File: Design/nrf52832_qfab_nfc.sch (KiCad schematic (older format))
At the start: 23 parts, among them U1 nRF52832_QFAB, X1 32MHz, X2 32.768kHz

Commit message: Improvement over the Power management: - added TPS6201DRC for raising leaking voltage from supercapacitor - supercap is protected from overvoltage using a shunt diode - power management is using MOSFET logic (2 PFET, 1 NFET)
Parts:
- renumbered C13 to C11, C14 to C12, C8 to C13, C3 to C14, C2 to C15, C1 to C16, C7 to C17, C6 to C18, C11 to C5, C12 to C6, C4 to C7, C9 to C8, C5 to C9, L2 to L4, L1 to L5, U1 to U3, X2 to X1, X1 to X2
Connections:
- net labels added: CPU_SWD_CLK, CPU_SWD_IO, CPU_SWD_~RESET~, CPU_UART_CTS, CPU_UART_RTS, CPU_UART_RX, CPU_UART_TX, Energy_NFC_1, Energy_NFC_2, LED_PWM_B, LED_PWM_G, LED_PWM_R, Memory_SPI_CLK, Memory_SPI_MISO, Memory_SPI_MOSI, Memory_SPI_~CS~, Memory_SPI_~HOLD~, Memory_SPI_~WP~
- wire segments 96 -> 100
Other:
- moved on the sheet: C_tune1

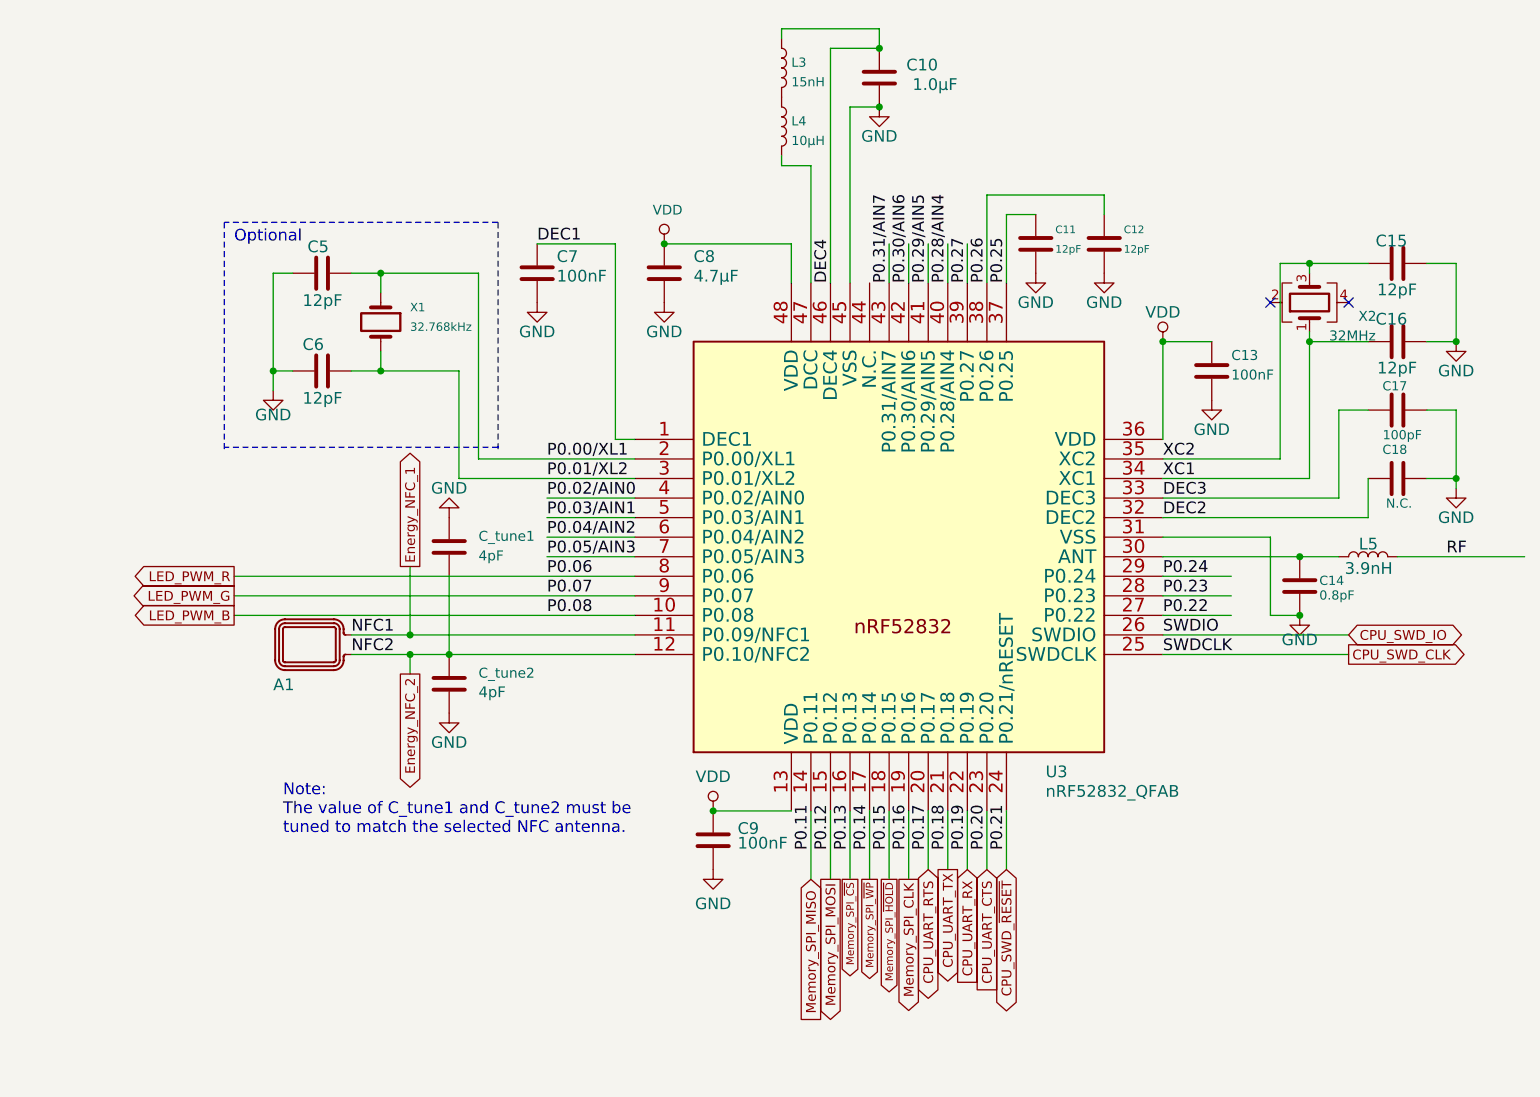
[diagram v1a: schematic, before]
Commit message: - designed configurable intensity for RGB LEDs - included Breakout (FET, Diode, etc.) Spice models from Cadence Spice - replaced global label with hierarchical complete view - customized net labels with pin function - exported first spice netlist which presents small bugs
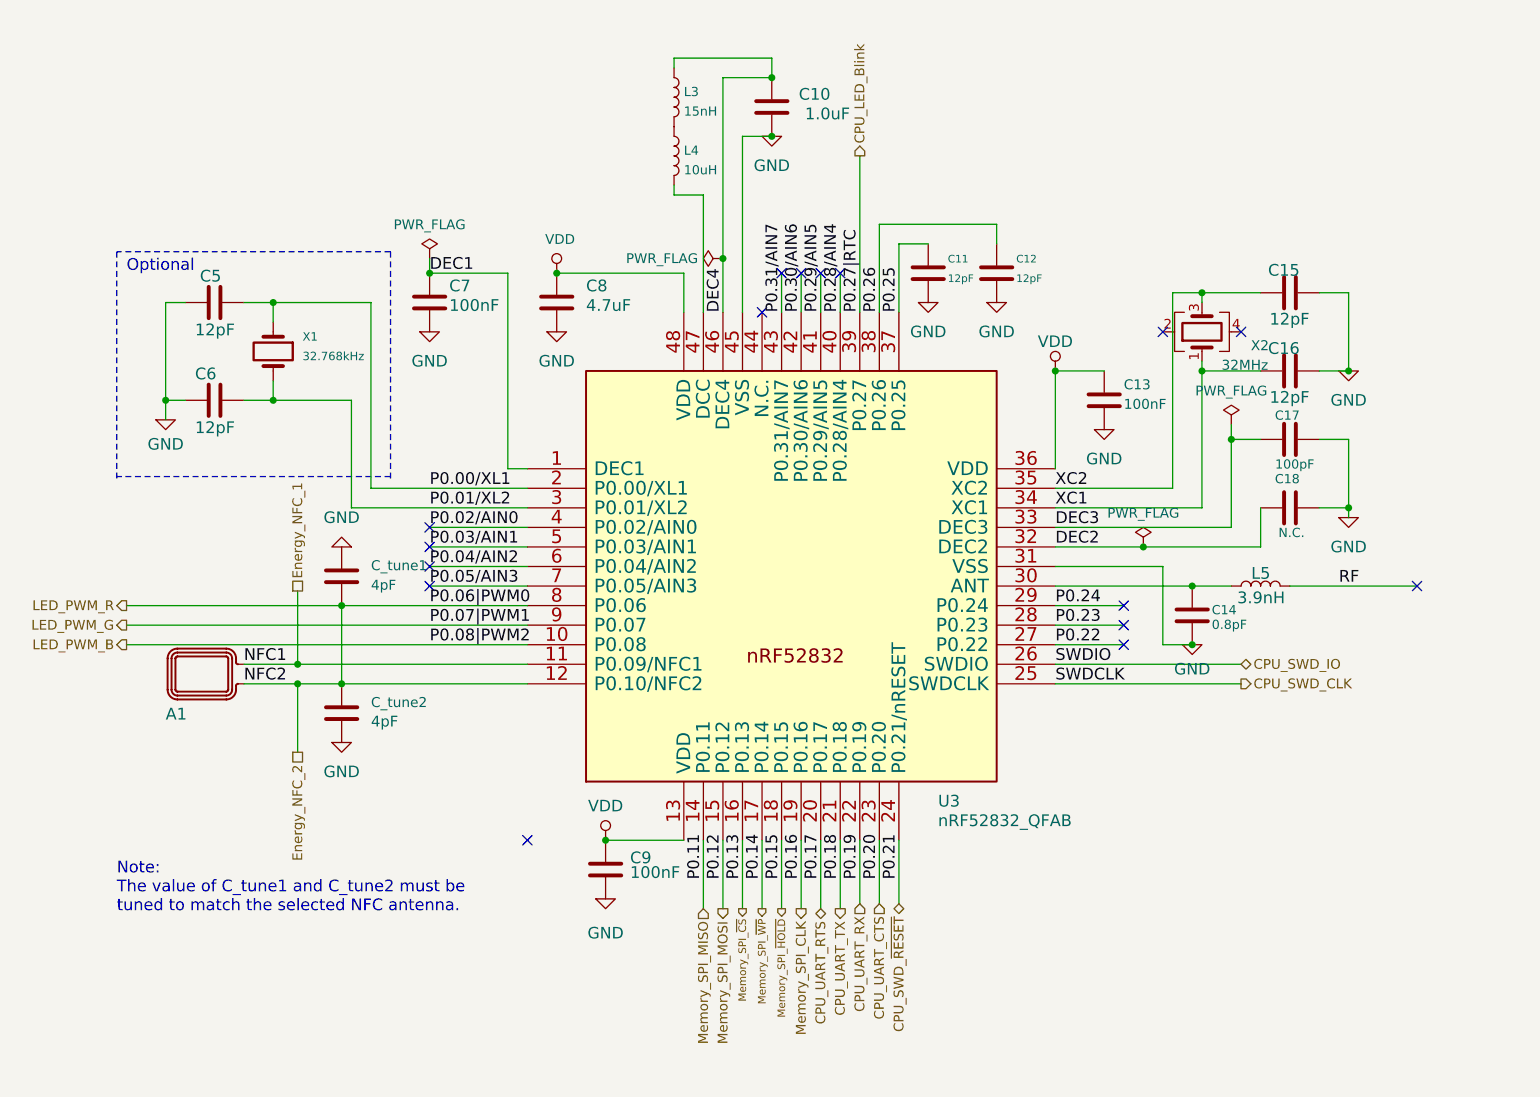
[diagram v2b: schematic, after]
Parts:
- A1: Spice_Model (none) -> 0; Spice_Netlist_Enabled (none) -> N; Spice_Primitive (none) -> L
- C10: value 1.0µF -> 1.0uF; Spice_Model (none) -> 1.0u; Spice_Netlist_Enabled (none) -> Y; Spice_Primitive (none) -> C
- C11, C12, C15, C16, C5, C6: Spice_Model (none) -> 12p; Spice_Netlist_Enabled (none) -> Y; Spice_Primitive (none) -> C
- C13, C7, C9: Spice_Model (none) -> 100n; Spice_Netlist_Enabled (none) -> Y; Spice_Primitive (none) -> C
- C14: Spice_Model (none) -> 0.8; Spice_Netlist_Enabled (none) -> Y; Spice_Primitive (none) -> C
- C17: Spice_Model (none) -> 100p; Spice_Netlist_Enabled (none) -> Y; Spice_Primitive (none) -> C
- C18: Spice_Model (none) -> 0; Spice_Netlist_Enabled (none) -> N; Spice_Primitive (none) -> C
- C8: value 4.7µF -> 4.7uF; Spice_Model (none) -> 4.7u; Spice_Netlist_Enabled (none) -> Y; Spice_Primitive (none) -> C
- C_tune1, C_tune2: Spice_Model (none) -> 4p; Spice_Netlist_Enabled (none) -> Y; Spice_Primitive (none) -> C
- L4: value 10µH -> 10uH; Spice_Model (none) -> 10u; Spice_Netlist_Enabled (none) -> Y; Spice_Primitive (none) -> L
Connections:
- net labels added: CPU_LED_Blink, P0.06|PWM0, P0.07|PWM1, P0.08|PWM2, P0.27|RTC
- net labels removed: P0.06, P0.07, P0.08, P0.27
- wire segments 100 -> 105
- no-connect marks 2 -> 16
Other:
- moved on the sheet: A1, C10, C11, C12, C13, C14, C15, C16, C17, C18, C5, C6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
